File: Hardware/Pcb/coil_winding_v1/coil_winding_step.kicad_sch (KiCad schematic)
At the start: 24 parts, among them J1 Conn_01x14_Pin, J2 Screw_Terminal_01x02, M1 Stepper_Motor_bipolar, M2 Stepper_Motor_bipolar, SW1 SW_SPST, SW2 SW_SPST, SW3 RotaryEncoder_Switch, U1 LM7805_TO220

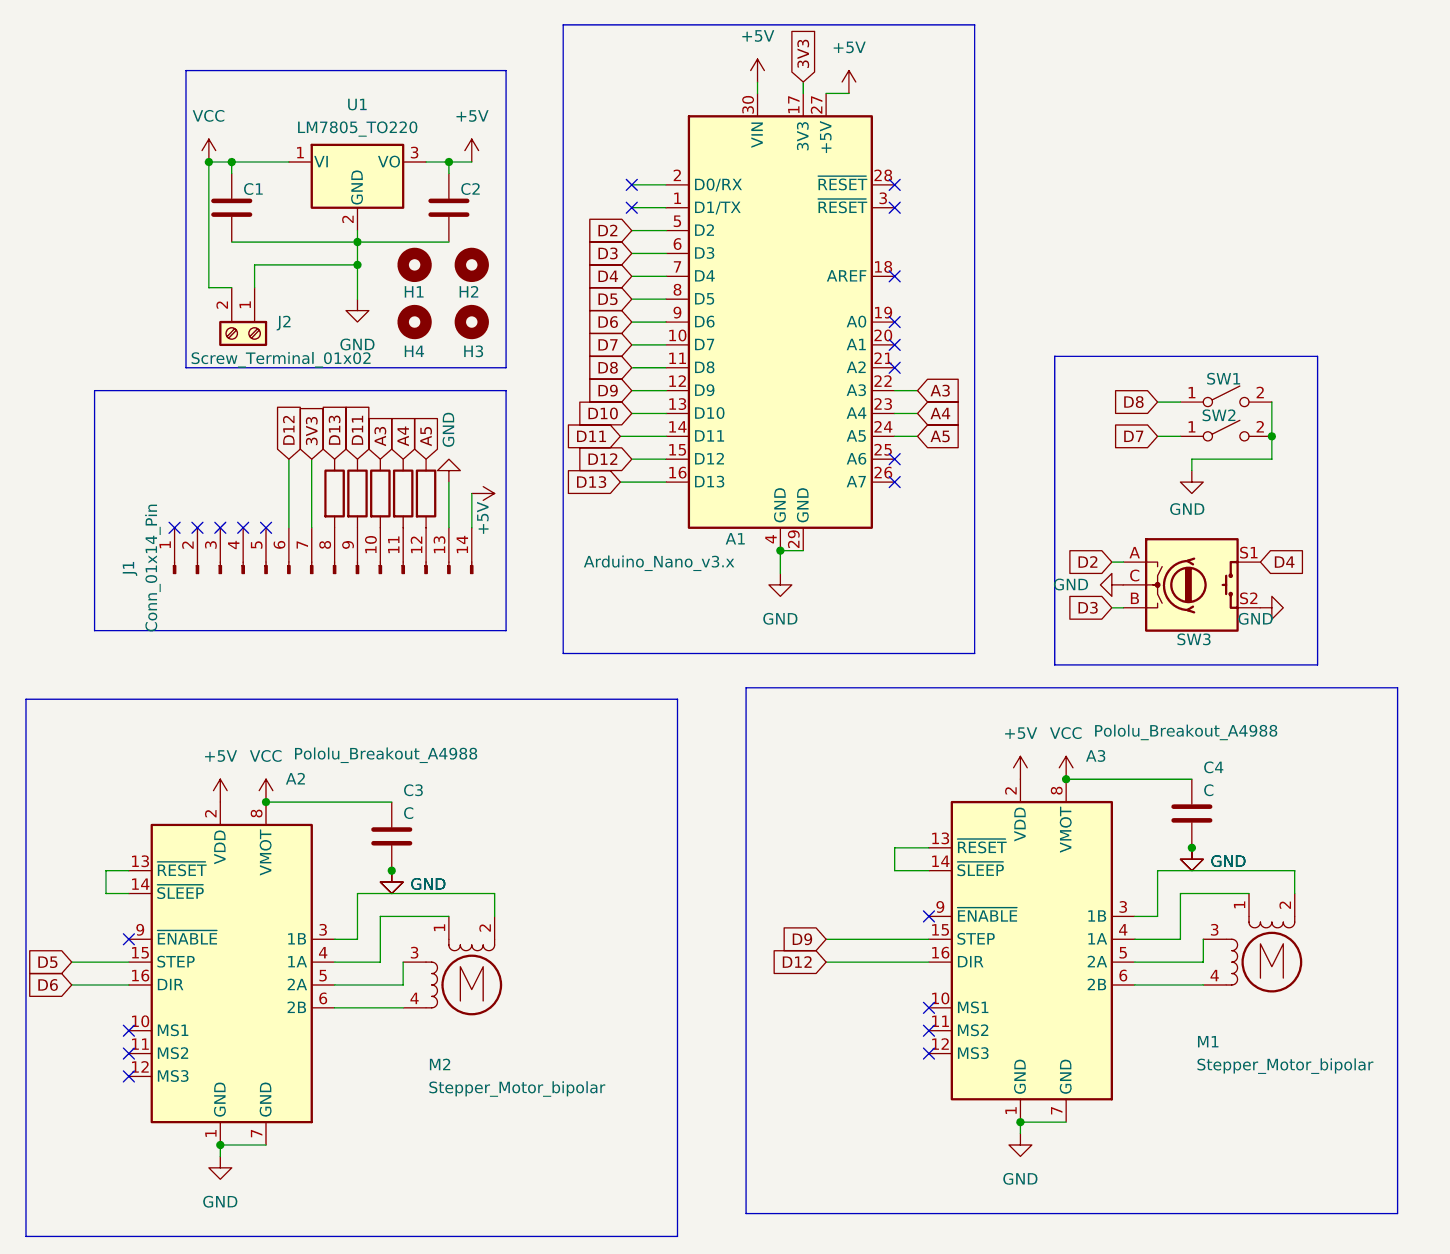
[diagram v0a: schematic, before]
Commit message: Update version-2 PCB: modified tracks and footprint
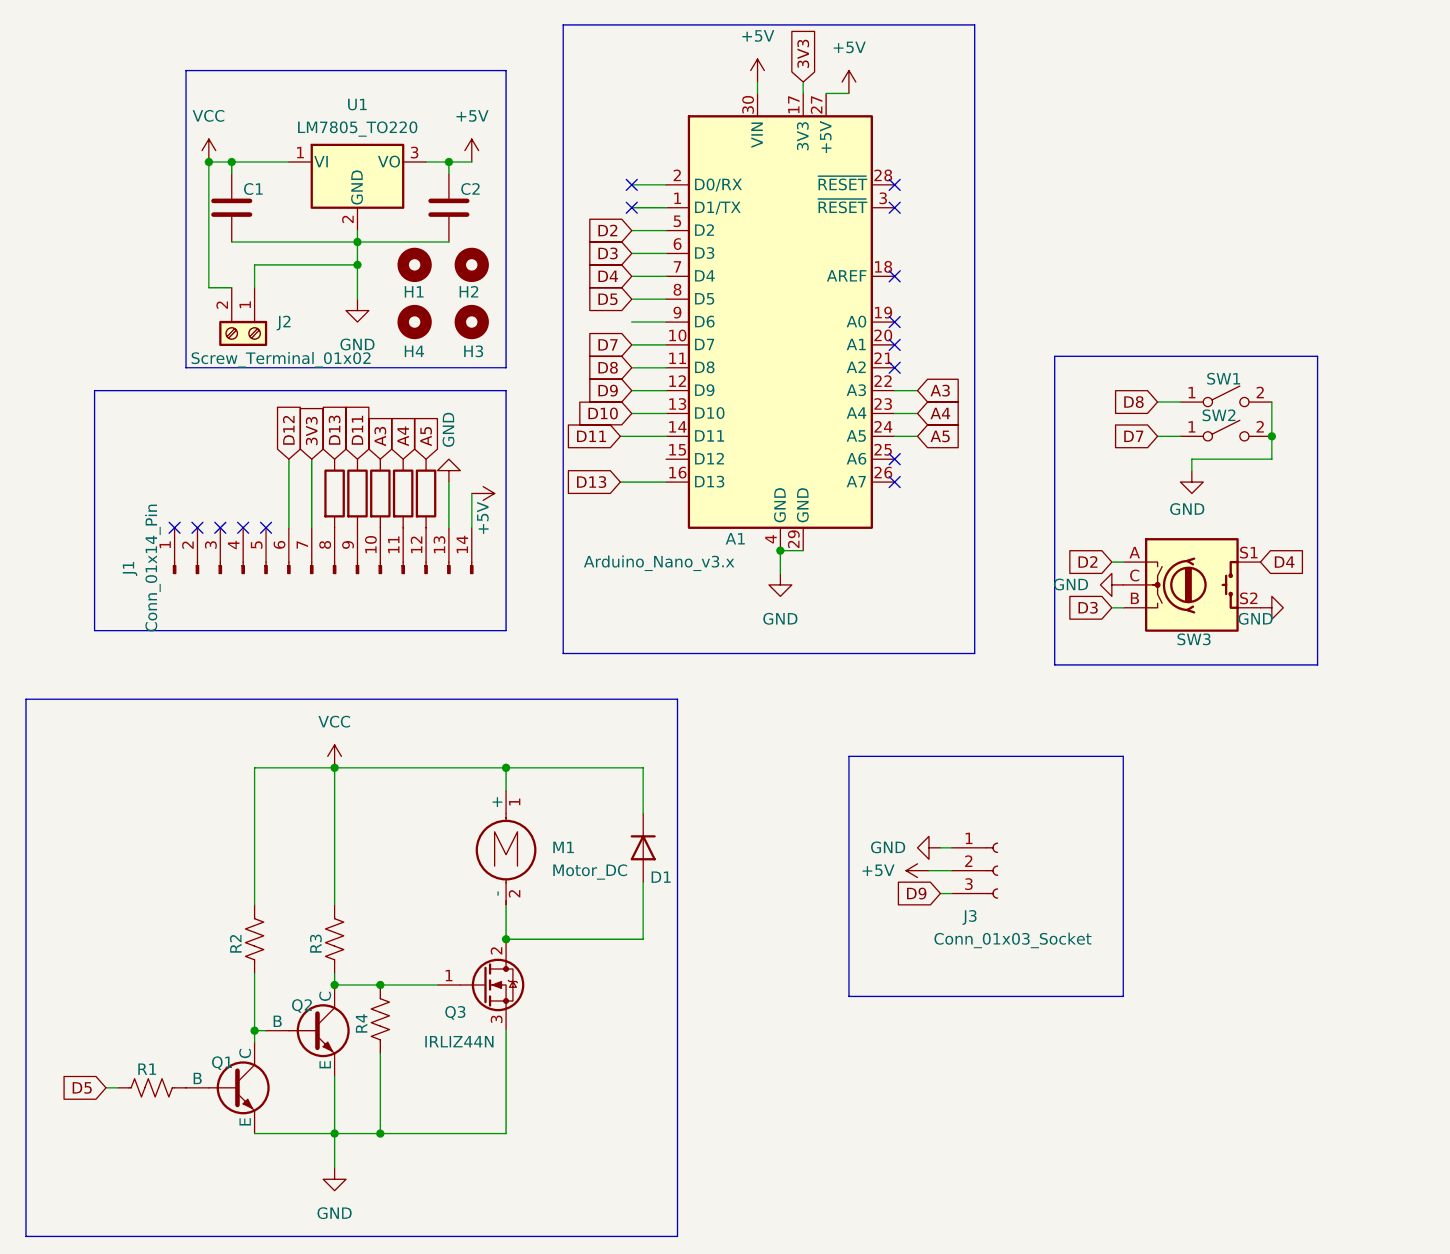
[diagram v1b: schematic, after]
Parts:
- removed A2, A3: Pololu_Breakout_A4988, Module:Pololu_Breakout-16_15.2x20.3mm, symbol Driver_Motor:Pololu_Breakout_A4988
- removed C3, C4: C, symbol Device:C
- removed M1, M2: Stepper_Motor_bipolar, symbol Motor:Stepper_Motor_bipolar
- added D1: D, Diode_THT:D_DO-41_SOD81_P12.70mm_Horizontal, symbol Device:D
- added J3: Conn_01x03_Socket, Connector_PinSocket_2.54mm:PinSocket_1x03_P2.54mm_Vertical, symbol Connector:Conn_01x03_Socket
- added M1: Motor_DC, Connector_PinHeader_2.54mm:PinHeader_1x02_P2.54mm_Vertical, symbol Motor:Motor_DC
- added Q1, Q2: NPN, Package_TO_SOT_THT:TO-92, symbol Simulation_SPICE:NPN
- added Q3: IRLIZ44N, Package_TO_SOT_THT:TO-220F-3_Vertical, symbol Transistor_FET:IRLIZ44N
- added R1, R2, R3, R4: R_US, Resistor_THT:R_Axial_DIN0207_L6.3mm_D2.5mm_P7.62mm_Horizontal, symbol Device:R_US
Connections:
- net +5V: now also J3.2 (Pin_2)
- net D12: no longer A1.15 (D12)
- net D5: now also R1.1
- net D9: now also J3.3 (Pin_3)
- net GND: now also J3.1 (Pin_1), Q1.3 (E), Q2.3 (E), Q3.3 (S), R4.1
- net VCC: now also D1.1 (K), M1.1 (+), R2.2, R3.2
- net D6: no longer names the net of A1.9 (D6)
- new net: Q2.1 (C), Q3.1 (G), R3.1, R4.2
- new net: D1.2 (A), M1.2 (-), Q3.2 (D)
- new net: Q1.1 (C), Q2.2 (B), R2.1
- new net: Q1.2 (B), R1.2
- no-connect marks 23 -> 15

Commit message: Changes made
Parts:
- SW3: footprint Rotary_Encoder:RotaryEncoder_Alps_EC11E_Vertical_H20mm_CircularMountingHoles -> Rotary_Encoder:RotaryEncoder_Alps_EC12E-Switch_Vertical_H20mm
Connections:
- no-connect marks 15 -> 14
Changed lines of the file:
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@@
 	)
 	(junction
+		(at 142.24 92.71)
+		(diameter 0)
+		(color 0 0 0 0)
+	)
+	(junction
 		(at 54.61 45.72)
 		(diameter 0)
@@
 	)
 	(no_connect
-		(at 128.27 66.04)
-	)
-	(no_connect
 		(at 58.42 86.36)
 	)
@@
 	(wire
 		(pts
-			(xy 99.06 58.42) (xy 102.87 58.42)
+			(xy 128.27 73.66) (xy 130.81 73.66)
 		)
 		(stroke
@@
 	(wire
 		(pts
-			(xy 128.27 73.66) (xy 130.81 73.66)
+			(xy 66.04 113.03) (xy 85.09 113.03)
 		)
 		(stroke
@@
 	(wire
 		(pts
-			(xy 66.04 113.03) (xy 85.09 113.03)
+			(xy 57.15 113.03) (xy 57.15 128.27)
 		)
 		(stroke
@@
 	(wire
 		(pts
-			(xy 57.15 113.03) (xy 57.15 128.27)
+			(xy 152.4 90.17) (xy 153.67 90.17)
 		)
 		(stroke
@@
 	(wire
 		(pts
-			(xy 152.4 90.17) (xy 153.67 90.17)
+			(xy 99.06 58.42) (xy 102.87 58.42)
 		)
 		(stroke
@@
 	(wire
 		(pts
+			(xy 140.97 92.71) (xy 142.24 92.71)
+		)
+		(stroke
+			(width 0)
+			(type default)
+		)
+	)
+	(wire
+		(pts
 			(xy 57.15 142.24) (xy 57.15 143.51)
 		)
@@
 	(wire
 		(pts
-			(xy 99.06 63.5) (xy 102.87 63.5)
+			(xy 142.24 100.33) (xy 168.91 100.33)
 		)
 		(stroke
@@
 	(wire
 		(pts
+			(xy 142.24 92.71) (xy 142.24 100.33)
+		)
+		(stroke
+			(width 0)
+			(type default)
+		)
+	)
+	(wire
+		(pts
 			(xy 76.2 45.72) (xy 78.74 45.72)
 		)
@@
 	(wire
 		(pts
+			(xy 175.26 90.17) (xy 168.91 90.17)
+		)
+		(stroke
+			(width 0)
+			(type default)
+		)
+	)
+	(wire
+		(pts
+			(xy 142.24 92.71) (xy 153.67 92.71)
+		)
+		(stroke
+			(width 0)
+			(type default)
+		)
+	)
+	(wire
+		(pts
 			(xy 113.03 36.83) (xy 113.03 38.1)
 		)
@@
 	(wire
 		(pts
+			(xy 168.91 100.33) (xy 168.91 95.25)
+		)
+		(stroke
+			(width 0)
+			(type default)
+		)
+	)
+	(wire
+		(pts
 			(xy 52.07 45.72) (xy 52.07 59.69)
 		)
@@
 		)
 	)
+	(global_label "D4"
+		(shape input)
+		(at 99.06 58.42 180)
+		(fields_autoplaced yes)
+		(effects
+			(font
+				(size 1.27 1.27)
+			)
+			(justify right)
+		)
+		(property "Intersheetrefs" "${INTERSHEET_REFS}"
+			(at 93.5953 58.42 0)
+			(effects
+				(font
+					(size 1.27 1.27)
+				)
+				(justify right)
+				(hide yes)
+			)
+		)
+	)
 	(global_label "D13"
 		(shape input)
@@
 		)
 	)
-	(global_label "A4"
+	(global_label "D4"
 		(shape input)
-		(at 130.81 73.66 0)
+		(at 175.26 90.17 0)
 		(fields_autoplaced yes)
 		(effects
@@
 		)
 		(property "Intersheetrefs" "${INTERSHEET_REFS}"
-			(at 136.0933 73.66 0)
+			(at 180.7247 90.17 0)
 			(effects
 				(font
@@
 		)
 	)
-	(global_label "D4"
+	(global_label "A4"
 		(shape input)
-		(at 99.06 58.42 180)
+		(at 130.81 73.66 0)
 		(fields_autoplaced yes)
 		(effects
@@
 				(size 1.27 1.27)
 			)
-			(justify right)
+			(justify left)
 		)
 		(property "Intersheetrefs" "${INTERSHEET_REFS}"
-			(at 93.5953 58.42 0)
+			(at 136.0933 73.66 0)
 			(effects
 				(font
 					(size 1.27 1.27)
 				)
-				(justify right)
+				(justify left)
 				(hide yes)
 			)
@@
 		)
 	)
-	(global_label "D4"
-		(shape input)
-		(at 168.91 90.17 0)
-		(fields_autoplaced yes)
-		(effects
-			(font
-				(size 1.27 1.27)
-			)
-			(justify left)
-		)
-		(property "Intersheetrefs" "${INTERSHEET_REFS}"
-			(at 174.3747 90.17 0)
-			(effects
-				(font
-					(size 1.27 1.27)
-				)
-				(justify left)
-				(hide yes)
-			)
-		)
-	)
 	(symbol
 		(lib_id "Device:R")
@@
 	(symbol
 		(lib_id "power:GND")
-		(at 153.67 92.71 270)
+		(at 140.97 92.71 270)
 		(unit 1)
 		(exclude_from_sim no)
@@
 		(fields_autoplaced yes)
 		(property "Reference" "#PWR018"
-			(at 147.32 92.71 0)
+			(at 134.62 92.71 0)
 			(effects
 				(font
@@
 		)
 		(property "Value" "GND"
-			(at 149.86 92.7099 90)
+			(at 137.16 92.7099 90)
 			(effects
 				(font
@@
 				)
 				(justify right)
+				(hide yes)
 			)
 		)
 		(property "Footprint" ""
-			(at 153.67 92.71 0)
+			(at 140.97 92.71 0)
 			(effects
 				(font
@@
 		)
 		(property "Datasheet" ""
-			(at 153.67 92.71 0)
+			(at 140.97 92.71 0)
 			(effects
 				(font
@@
 		)
 		(property "Description" "Power symbol creates a global label with name \"GND\" , ground"
-			(at 153.67 92.71 0)
+			(at 140.97 92.71 0)
 			(effects
 				(font
@@
 	)
 	(symbol
-		(lib_id "power:GND")
-		(at 168.91 95.25 90)
-		(unit 1)
-		(exclude_from_sim no)
-		(in_bom yes)
-		(on_board yes)
-		(dnp no)
-		(property "Reference" "#PWR019"
-			(at 175.26 95.25 0)
-			(effects
-				(font
-					(size 1.27 1.27)
-				)
-				(hide yes)
-			)
-		)
-		(property "Value" "GND"
-			(at 166.37 96.52 90)
-			(effects
-				(font
-					(size 1.27 1.27)
-				)
-				(justify right)
-			)
-		)
-		(property "Footprint" ""
-			(at 168.91 95.25 0)
-			(effects
-				(font
-					(size 1.27 1.27)
-				)
-				(hide yes)
-			)
-		)
-		(property "Datasheet" ""
-			(at 168.91 95.25 0)
-			(effects
-				(font
-					(size 1.27 1.27)
-				)
-				(hide yes)
-			)
-		)
-		(property "Description" "Power symbol creates a global label with name \"GND\" , ground"
-			(at 168.91 95.25 0)
-			(effects
-				(font
-					(size 1.27 1.27)
-				)
-				(hide yes)
-			)
-		)
-		(pin "1"
-		)
-		(instances
-			(project "coil_winding"
-				(path "/b28ec357-7924-445c-8320-f5bf00c8aa67"
-					(reference "#PWR019")
-					(unit 1)
-				)
-			)
-		)
-	)
-	(symbol
 		(lib_id "Mechanical:MountingHole")
 		(at 81.28 63.5 0)
@@
 			)
 		)
-		(property "Footprint" "Rotary_Encoder:RotaryEncoder_Alps_EC11E_Vertical_H20mm_CircularMountingHoles"
+		(property "Footprint" "Rotary_Encoder:RotaryEncoder_Alps_EC12E-Switch_Vertical_H20mm"
 			(at 157.48 88.646 0)
 			(effects
